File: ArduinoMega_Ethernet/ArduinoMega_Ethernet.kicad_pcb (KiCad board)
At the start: 2 copper layers, 101.6 x 53.3 mm, 88 parts, among them J1 RJ45_Amphenol_RJMG1BD3B8K1ANR, J11 Micro_SD_Card_Det_Hirose_DM3AT, J9 PROGRAM_POWER_USBC, SW1 RST_BTN, U1 ATmega2560-16A, U2 CH340C, U3 ISM330DHCX, U4 W5500, U5 LM3281, U6 74HC244, U7 SE050C2HQ1, Y1 25Mhz, Y2 25Mhz

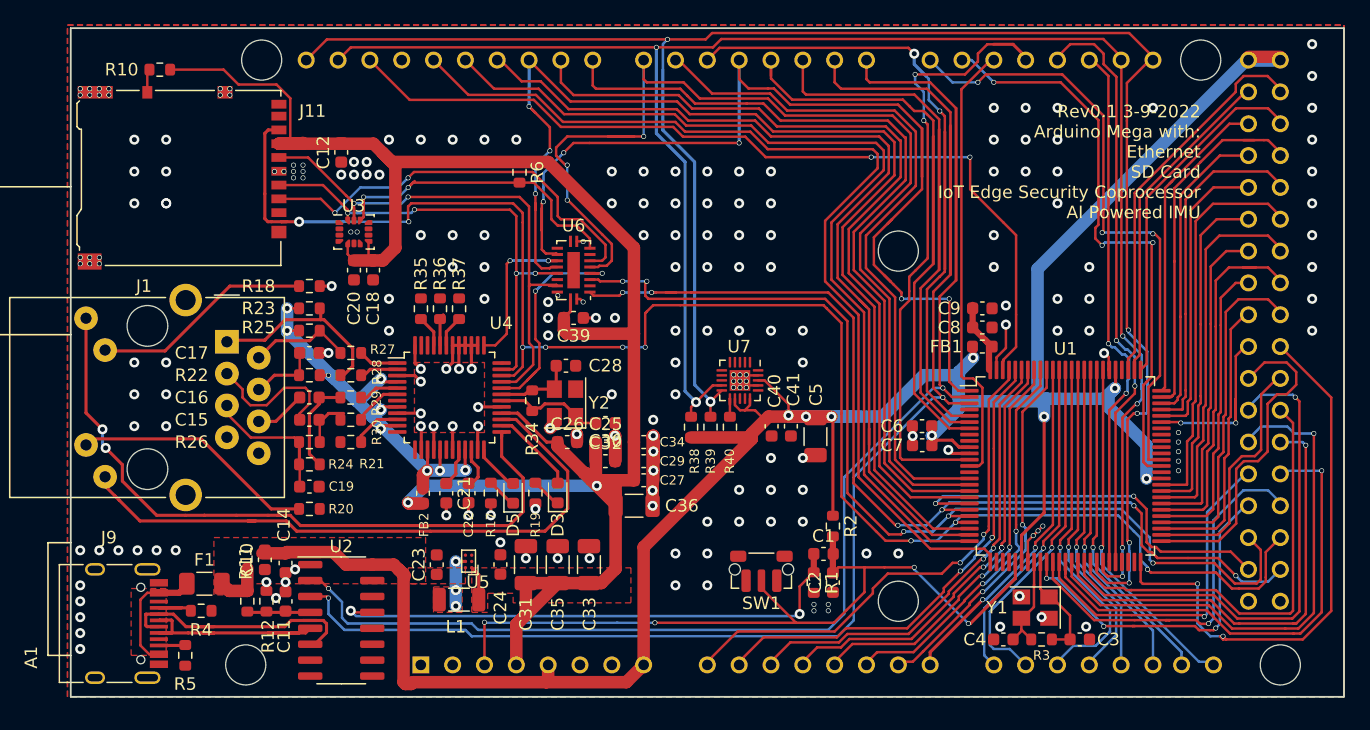
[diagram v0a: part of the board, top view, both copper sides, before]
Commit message: add usb protection, fix ioref
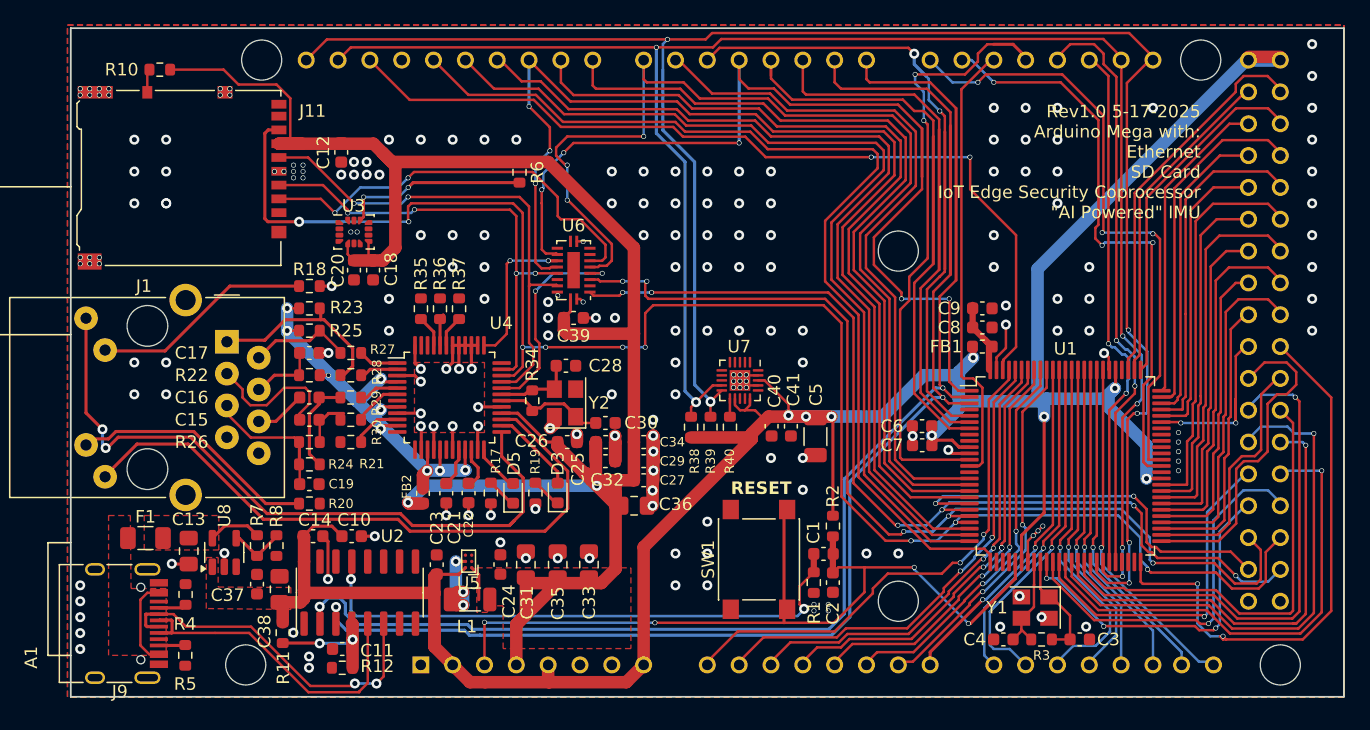
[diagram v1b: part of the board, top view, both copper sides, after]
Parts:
- added C13: 10uF, Capacitor_SMD:C_0805_2012Metric_Pad1.18x1.45mm_HandSolder, F.Cu at (52.6, 170.0)
- added C37: 100nF, Capacitor_SMD:C_0603_1608Metric, F.Cu at (58.0, 172.6)
- added C38: 10uF, Capacitor_SMD:C_0805_2012Metric_Pad1.18x1.45mm_HandSolder, F.Cu at (59.9, 173.0)
- added R7: 5.1k, Resistor_SMD:R_0603_1608Metric, F.Cu at (58.0, 169.6)
- added R8: DNP, Resistor_SMD:R_0603_1608Metric, F.Cu at (59.6, 169.6)
- added U8: AP22804AW5, Package_TO_SOT_SMD:SOT-23-5, F.Cu at (55.4, 170.1)
- C31, C33, C35, C36: footprint Capacitor_SMD:C_1206_3216Metric -> Capacitor_SMD:C_0805_2012Metric_Pad1.18x1.45mm_HandSolder
- SW1: footprint Button_Switch_SMD:SW_Push_1P1T-MP_NO_Horizontal_Alps_SKRTLAE010 -> Button_Switch_SMD:SW_SPST_PTS645
- Y1: value 25Mhz -> 16Mhz
- moved R12 8.05 mm to (64.8, 179.3), turned to 0 degrees
- moved C10 7.18 mm to (65.6, 168.8), turned to 180 degrees
- moved F1 5.94 mm to (49.1, 168.9)
- moved C11 5.91 mm to (64.8, 177.8), turned to 0 degrees
- moved R11 3.78 mm to (60.1, 176.5)
- moved C14 3.07 mm to (62.5, 168.8), turned to 180 degrees
- moved U2 2.66 mm to (66.2, 173.3), turned to 90 degrees
- moved R4 1.80 mm to (52.4, 173.4), turned to -90 degrees
- moved L1 0.88 mm to (75.0, 173.8)
- moved SW1 0.82 mm to (98.1, 170.7), turned to 90 degrees
- moved R20 0.42 mm to (62.2, 166.2)
- moved C19 0.20 mm to (62.2, 164.7)
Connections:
- net /PWRandPRG/USBC_VIN_CC1 renamed /PWRandPRG/USBC_CC1
- net /PWRandPRG/USBC_VIN_CC2 renamed /PWRandPRG/USBC_CC2
- net /PWRandPRG/USBC_VIN_DM renamed /PWRandPRG/USBC_D+
- net /PWRandPRG/USBC_VIN_DP renamed /PWRandPRG/USBC_D-
- A1 pad IOREF: /IOREF1 -> +5V
- F1 pad 1: +5V -> /PWRandPRG/USBC_VBUS
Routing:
- net Net-(U3-CS): track 25.8 -> 15.9 mm
- net /PWRandPRG/USBC_D+: track 19.2 -> 26.8 mm
- net GND: track 61.8 -> 68.4 mm, vias 216 -> 206
- net /PWRandPRG/USBC_D-: track 22.1 -> 27.9 mm, vias 0 -> 2
- net Net-(U2-V3): track 4.41 -> 9.26 mm, vias 0 -> 2
- net /MCU_RESET: track 63.6 -> 68.3 mm
- net Net-(U8-EN): track 0.00 -> 4.54 mm
- net /PWRandPRG/USBC_VBUS: track 0.00 -> 4.28 mm
- net /PIN_D4/CS2: track 80.7 -> 77.0 mm
- net Net-(U5-SW): track 4.32 -> 8.03 mm
- net /PIN_D11: track 76.0 -> 73.0 mm
- net /PWRandPRG/ETHERNET_SCLK: track 43.0 -> 40.2 mm
- net Net-(F1-Pad2): track 9.59 -> 7.12 mm
- net /PWRandPRG/PROGRAM_~{DTR}: track 43.1 -> 45.6 mm
- net /IOTSEC_SCL: track 153.3 -> 151.0 mm
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- added copper zone on F.Cu, net /PWRandPRG/USBC_VBUS
- removed copper zone on F.Cu, net Net-(U5-SW)
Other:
- board text added: "RESET"
- board text added: "Rev1.0 5-17-2025 Arduino Mega with: Ethernet SD Card IoT Edge Security Coprocessor {dblquote}AI Powered{dblquote} IMU"
- board text removed: "Rev0.1 3-9-2022 Arduino Mega with: Ethernet SD Card IoT Edge Security Coprocessor AI Powered IMU"

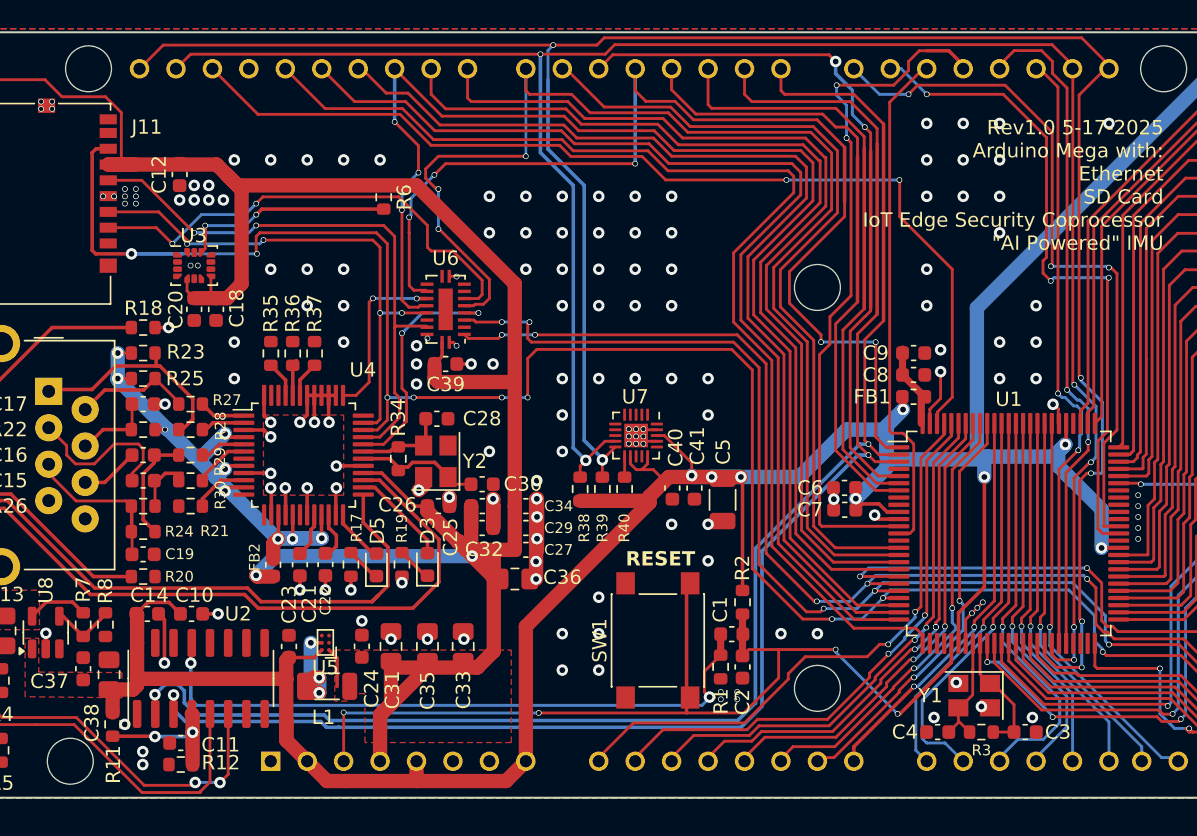
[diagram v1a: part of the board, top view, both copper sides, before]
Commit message: Fix IMU I2C, add SD Detect, Fix IoT CoPro Power
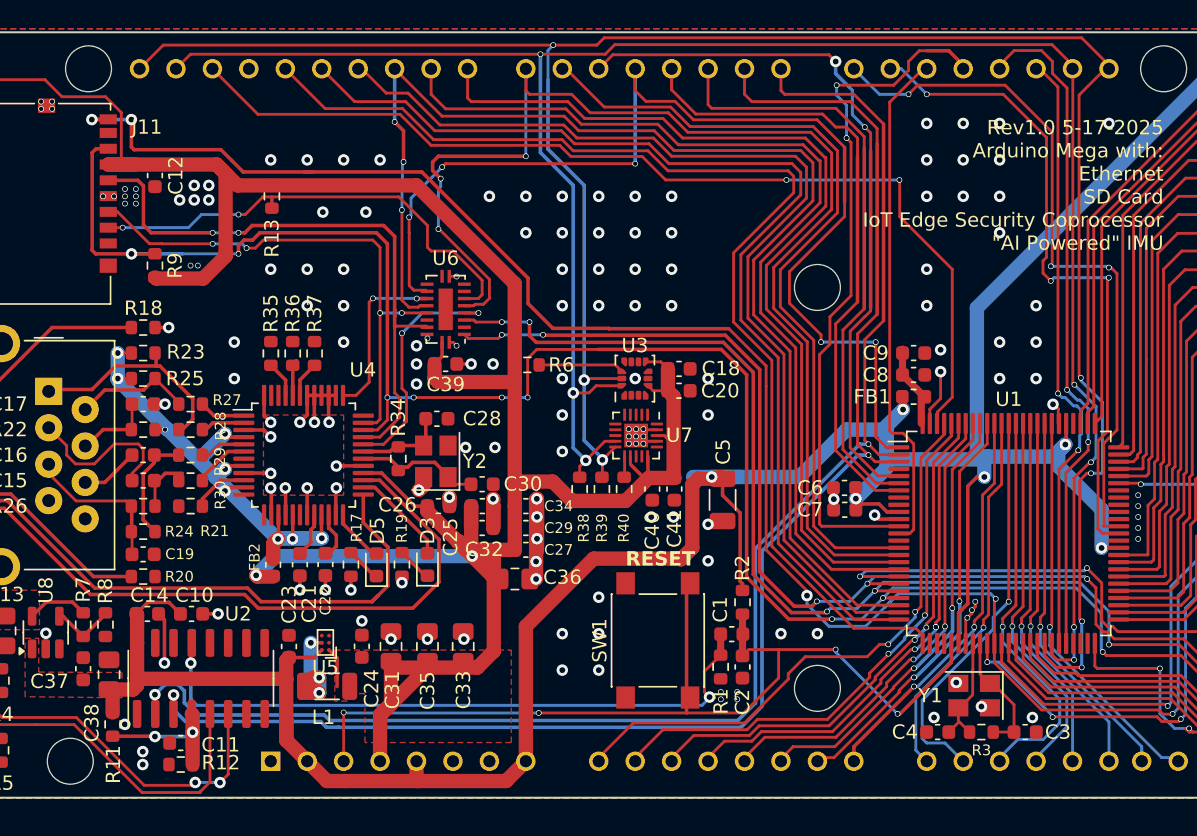
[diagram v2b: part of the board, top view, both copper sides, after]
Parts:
- added R13: 10k, Resistor_SMD:R_0603_1608Metric, F.Cu at (71.2, 139.7)
- added R9: 10k, Resistor_SMD:R_0603_1608Metric, F.Cu at (63.0, 144.5)
- moved C20 34.3 mm to (99.6, 153.2), turned to 180 degrees
- moved C18 32.5 mm to (99.6, 151.7), turned to 180 degrees
- moved U3 31.7 mm to (96.5, 152.4), turned to 90 degrees
- moved R6 15.4 mm to (89.0, 151.4), turned to 0 degrees
- moved C12 1.72 mm to (63.0, 138.2)
- moved C40 1.40 mm to (97.7, 160.1)
- moved C41 1.40 mm to (99.2, 160.1)
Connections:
- C40 pad 1: +5V -> +3V3
- C41 pad 1: +5V -> +3V3
- J11 pad 9: /PWRandPRG/SDCARD_DET -> /PIN_D48
- R38 pad 1: +5V -> +3V3
- R39 pad 1: +5V -> +3V3
- R40 pad 1: +5V -> +3V3
- U3 pad 13: /PWRandPRG/IMU_SCL -> /IOTSEC_SCL
- U3 pad 14: /PWRandPRG/IMU_SDA -> /IOTSEC_SDA
- U7 pad 12: +5V -> +3V3
- U7 pad 15: +5V -> +3V3
- U7 pad 18: +5V -> +3V3
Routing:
- net /PIN_D48: track 30.4 -> 125.2 mm, vias 1 -> 5
- net +3V3: track 165.8 -> 198.1 mm
- net +5V: track 214.8 -> 202.8 mm, vias 8 -> 6
- net Net-(U3-CS): track 15.9 -> 5.95 mm, vias 2 -> 0
- net /IOTSEC_SDA: track 142.6 -> 146.2 mm, vias 6 -> 7
- net /IOTSEC_SCL: track 151.0 -> 153.9 mm, vias 6 -> 7
- net /PIN_D50: track 132.6 -> 134.4 mm
- net /PWRandPRG/ETHERNET_SCLK: track 40.2 -> 41.8 mm
- net /ETHER_CS: track 89.6 -> 88.7 mm
- net /PIN_D52: track 78.2 -> 78.9 mm
- net GND: track 68.4 -> 68.2 mm, vias 206 -> 203

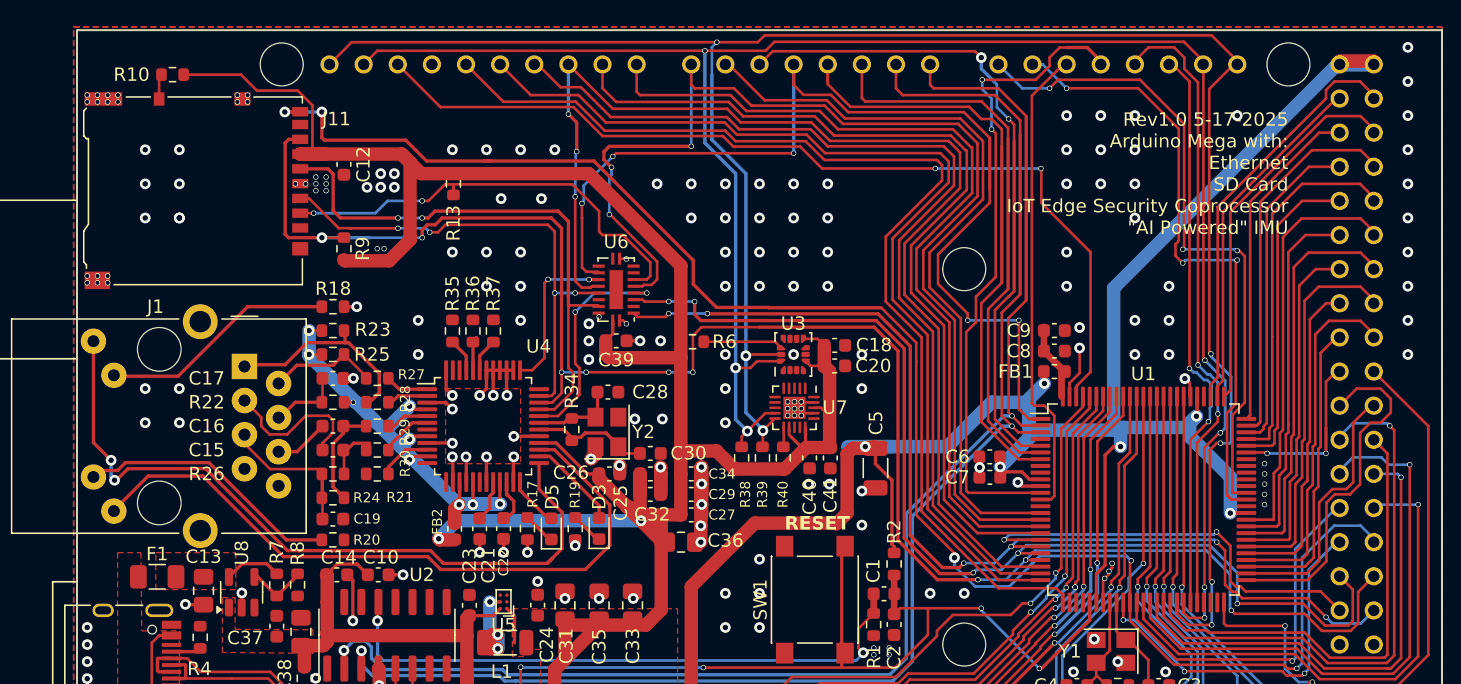
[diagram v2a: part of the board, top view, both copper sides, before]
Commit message: configurable io jumpers
configurable io jumpers
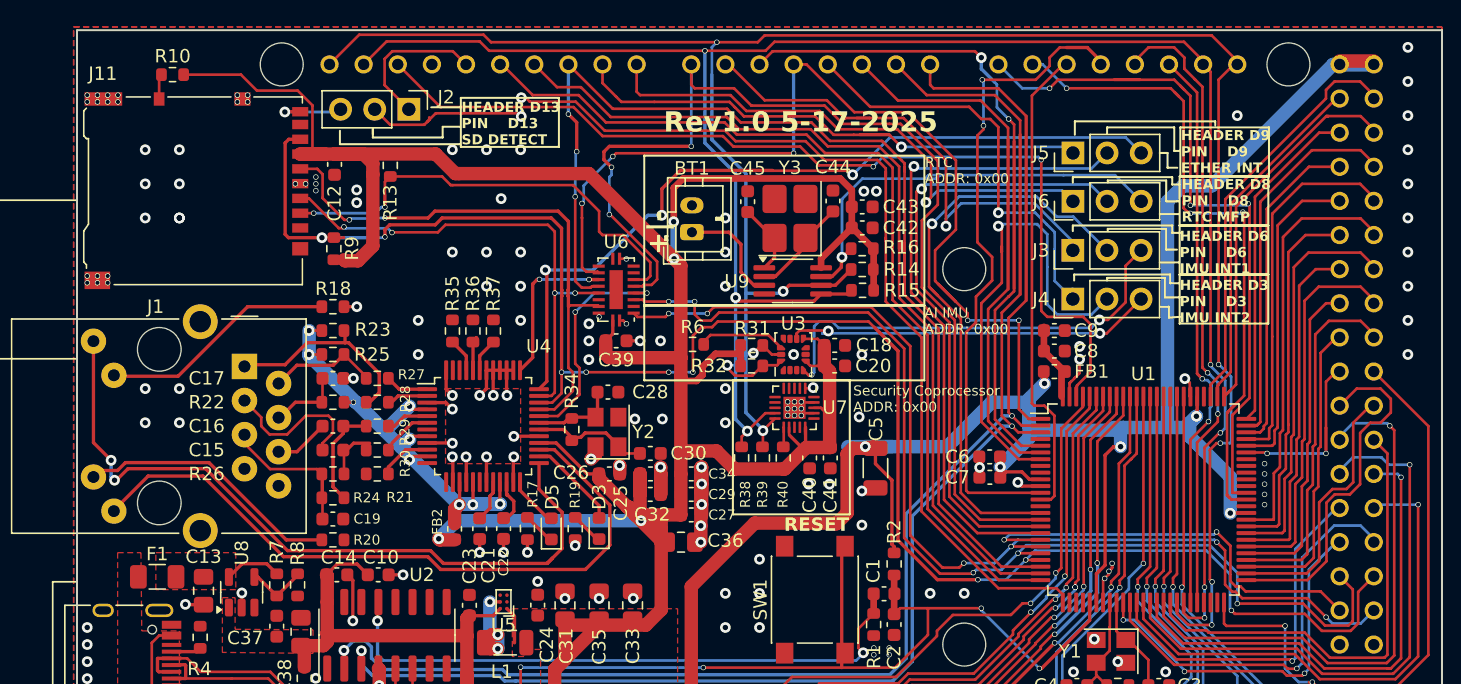
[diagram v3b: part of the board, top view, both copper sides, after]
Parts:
- added BT1: Battery_Cell, Connector_JST:JST_PH_B2B-PH-K_1x02_P2.00mm_Vertical, F.Cu at (89.0, 143.3)
- added C42: 100nF, Capacitor_SMD:C_0603_1608Metric, F.Cu at (101.6, 143.0)
- added C43: 100nF, Capacitor_SMD:C_0603_1608Metric, F.Cu at (101.6, 141.4)
- added C44: TBD, Capacitor_SMD:C_0603_1608Metric, F.Cu at (99.5, 141.0)
- added C45: TBD, Capacitor_SMD:C_0603_1608Metric, F.Cu at (93.1, 141.0)
- added J2: SD_DET_JUMP, Connector_PinHeader_2.54mm:PinHeader_1x03_P2.54mm_Vertical, F.Cu at (67.9, 134.2)
- added J3: IMU_INT1_JUMP, Connector_PinHeader_2.54mm:PinHeader_1x03_P2.54mm_Vertical, F.Cu at (117.3, 144.7)
- added J4: IMU_INT2_JUMP, Connector_PinHeader_2.54mm:PinHeader_1x03_P2.54mm_Vertical, F.Cu at (117.3, 148.3)
- added J5: ETHER_INT_JUMP, Connector_PinHeader_2.54mm:PinHeader_1x03_P2.54mm_Vertical, F.Cu at (117.3, 137.4)
- added J6: RTC_MFP_JUMP, Connector_PinHeader_2.54mm:PinHeader_1x03_P2.54mm_Vertical, F.Cu at (117.3, 141.0)
- added R14: 4.7k, Resistor_SMD:R_0603_1608Metric, F.Cu at (101.6, 146.1)
- added R15: 4.7k, Resistor_SMD:R_0603_1608Metric, F.Cu at (101.7, 147.6)
- added R16: 4.7k, Resistor_SMD:R_0603_1608Metric, F.Cu at (101.6, 144.5)
- added R31: 4.7k, Resistor_SMD:R_0603_1608Metric, F.Cu at (93.4, 151.7)
- added R32: 4.7k, Resistor_SMD:R_0603_1608Metric, F.Cu at (93.4, 153.2)
- added U9: MCP7940N-xST, Package_SO:MSOP-8_3x3mm_P0.65mm, F.Cu at (96.5, 146.9)
- added Y3: Crystal_GND23, Crystal:Crystal_SMD_3225-4Pin_3.2x2.5mm_HandSoldering, F.Cu at (96.2, 142.3)
- moved R13 4.90 mm to (66.5, 138.3)
- moved R9 0.75 mm to (62.3, 144.5)
- moved C12 0.70 mm to (62.4, 138.2)
- moved R6 0.20 mm to (89.0, 151.7)
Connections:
- net /IOTSEC_SCL renamed /PIN_D21
- net /IOTSEC_SDA renamed /PIN_D20
- net /PWRandPRG/ISM_I2C_MASTER_SCL renamed /PWRandPRG/ISM_I2C_M_SCL
- net /PWRandPRG/ISM_I2C_MASTER_SDA renamed /PWRandPRG/ISM_I2C_M_SDA
- A1 pad 13: /PIN_D13 -> /HEAD_D13
- A1 pad 3: /PIN_D3 -> /HEAD_D3
- A1 pad 6: /PIN_D6 -> /HEAD_D6
- A1 pad 8: /PIN_D8 -> /HEAD_D8
- A1 pad 9: /PIN_D9 -> /HEAD_D9
- J11 pad 9: /PIN_D48 -> /SD_DET
- U3 pad 4: /PWRandPRG/IMU_INT1 -> /IMU_INT1
- U3 pad 9: /PWRandPRG/IMU_INT2 -> /IMU_INT2
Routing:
- net /PIN_D48: track 125.2 -> 30.4 mm, vias 5 -> 1
- net /ETHER_~{INT}: track 0.00 -> 59.5 mm, vias 0 -> 3
- net /HEAD_D9: track 0.00 -> 40.9 mm, vias 0 -> 1
- net /HEAD_D8: track 0.00 -> 40.9 mm, vias 0 -> 1
- net /HEAD_D6: track 0.00 -> 38.1 mm, vias 0 -> 1
- net +3V3: track 198.1 -> 236.2 mm, vias 2 -> 4
- net /IMU_INT1: track 0.00 -> 33.1 mm, vias 0 -> 2
- net /RTC_MFP: track 0.00 -> 32.7 mm, vias 0 -> 1
- net /HEAD_D3: track 0.00 -> 32.1 mm, vias 0 -> 1
- net /IMU_INT2: track 0.00 -> 27.8 mm, vias 0 -> 2
- net /PIN_D8: track 65.1 -> 46.3 mm, vias 0 -> 1
- net /PIN_D9: track 67.7 -> 49.0 mm, vias 0 -> 1
- net /PIN_D6: track 57.0 -> 44.0 mm, vias 0 -> 1
- net /PIN_D20: track 146.2 -> 157.6 mm, vias 7 -> 8
- net /HEAD_D13: track 0.00 -> 11.2 mm
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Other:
- board text added: "+|-"
- board text added: "AI IMU ADDR: 0x00"
- board text added: "HEADER D13 PIN D13 SD DETECT"
- board text added: "HEADER D3 PIN D3 IMU INT2"
- board text added: "HEADER D6 PIN D6 IMU INT1"
- board text added: "HEADER D8 PIN D8 RTC MFP"
- board text added: "HEADER D9 PIN D9 ETHER INT"
- board text added: "RTC ADDR: 0x00"
- board text added: "Rev1.0 5-17-2025"
- board text added: "Security Coprocessor ADDR: 0x00"
- board text removed: "Rev1.0 5-17-2025 Arduino Mega with: Ethernet SD Card IoT Edge Security Coprocessor {dblquote}AI Powered{dblquote} IMU"
